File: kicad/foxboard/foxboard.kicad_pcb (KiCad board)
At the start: 2 copper layers, 360.7 x 139.7 mm, 183 parts, among them J2 USB_C_Receptacle_USB2.0, K1 KEYSW, K10 KEYSW, K11 KEYSW, K12 KEYSW, K13 KEYSW, K14 KEYSW, K15 KEYSW, K16 KEYSW, K17 KEYSW, K18 KEYSW, K19 KEYSW, K2 KEYSW, K20 KEYSW, K21 KEYSW, K22 KEYSW, K23 KEYSW, K24 KEYSW, K25 KEYSW, K26 KEYSW, K27 KEYSW, K28 KEYSW, K29 KEYSW, K3 KEYSW, K30 KEYSW, K31 KEYSW, K32 KEYSW, K33 KEYSW, K34 KEYSW, K35 KEYSW, K36 KEYSW, K37 KEYSW, K38 KEYSW, K39 KEYSW, K4 KEYSW, K40 KEYSW, K41 KEYSW, K42 KEYSW, K43 KEYSW, K44 KEYSW, K45 KEYSW, K46 KEYSW, K47 KEYSW, K48 KEYSW, K49 KEYSW, K5 KEYSW, K50 KEYSW, K51 KEYSW, K52 KEYSW, K53 KEYSW, K54 KEYSW, K55 KEYSW, K56 KEYSW, K57 KEYSW, K58 KEYSW, K59 KEYSW, K6 KEYSW, K60 KEYSW, K61 KEYSW, K62 KEYSW, K63 KEYSW, K64 KEYSW, K65 KEYSW, K66 KEYSW, K67 KEYSW, K68 KEYSW, K69 KEYSW, K7 KEYSW, K70 KEYSW, K71 KEYSW, K72 KEYSW, K73 KEYSW, K74 KEYSW, K75 KEYSW, K76 KEYSW, K77 KEYSW, K78 KEYSW, K79 KEYSW, K8 KEYSW, K80 KEYSW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

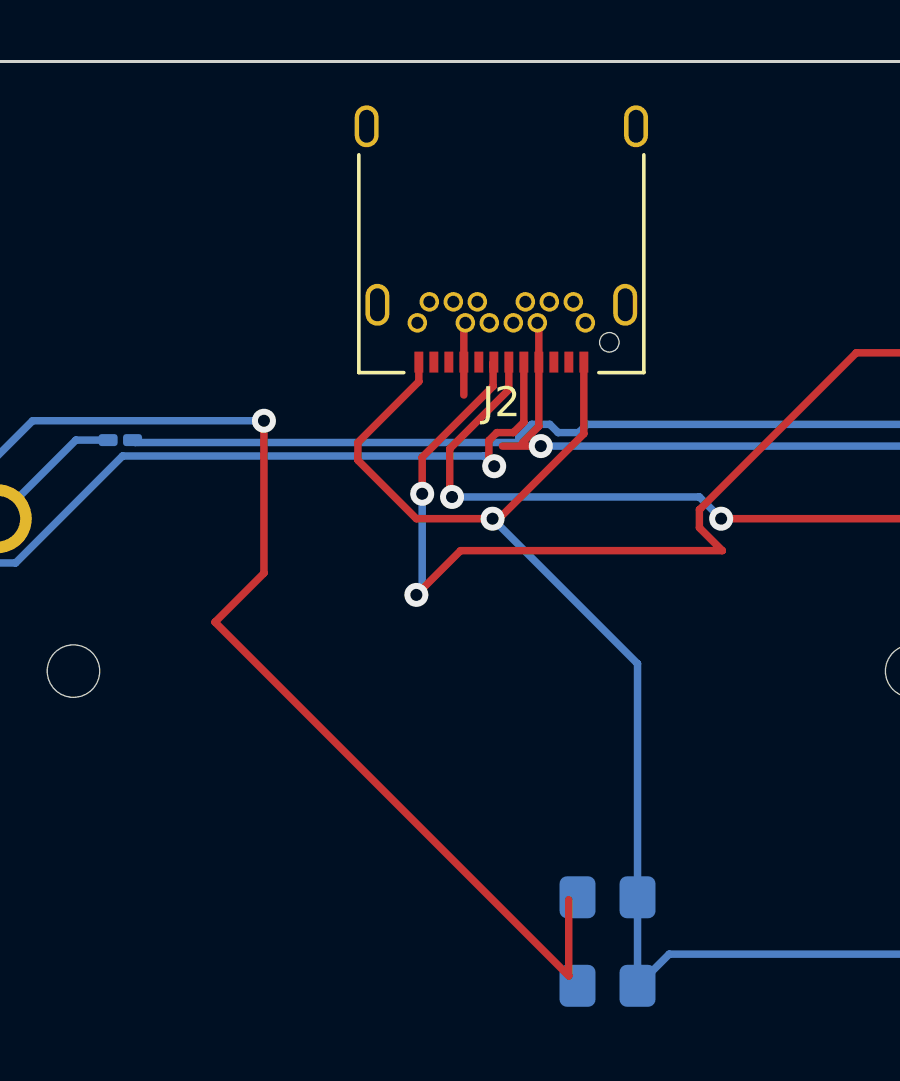
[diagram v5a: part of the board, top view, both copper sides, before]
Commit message: use usbc 2.0 recepticale
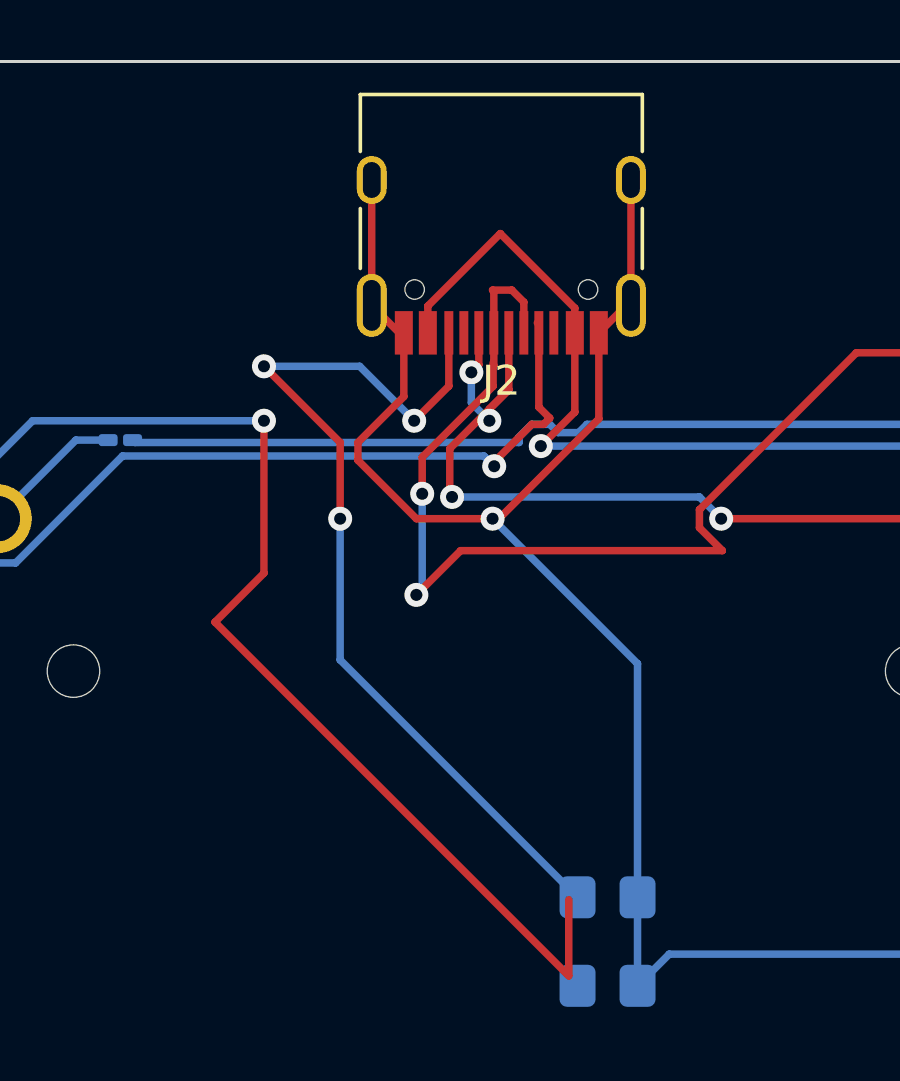
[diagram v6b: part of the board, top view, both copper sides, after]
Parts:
- J2: footprint Connector_USB:USB_C_Receptacle_Amphenol_12401548E4-2A -> Connector_USB:USB_C_Receptacle_HRO_TYPE-C-31-M-12
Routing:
- net Net-(J2-CC2): track 0.00 -> 31.2 mm, vias 0 -> 3
- net GND: track 402.1 -> 415.3 mm
- net Net-(J2-D+-PadA6): track 400.7 -> 406.3 mm, vias 3 -> 5
- net VBUS: track 405.5 -> 410.4 mm
- net Net-(J2-D--PadA7): track 424.7 -> 429.5 mm
- net Net-(J2-CC1): track 63.7 -> 65.0 mm

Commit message: add fill
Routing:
- net row 2: track 401.6 -> 403.5 mm
- net Net-(J2-CC1): track 65.0 -> 64.8 mm, vias 2 -> 3
- added copper zone on F.Cu, net GND

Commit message: update
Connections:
- U2 pad 43: unconnected-(U2-21_A7_RX5_BCLK1-Pad43) -> row 3
- U2 pad 44: row 3 -> row 2
- U2 pad 45: row 2 -> row 1
- U2 pad 46: row 1 -> unconnected-(U2-3V3-Pad46)
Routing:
- net row 2: track 403.5 -> 405.9 mm
- net row 1: track 419.9 -> 421.3 mm
- net row 3: track 392.6 -> 393.5 mm
- net VBUS: track 410.4 -> 410.5 mm, vias 3 -> 4
- added copper zone on B.Cu, net GND
- added copper zone on F.Cu, net VBUS
- removed copper zone on F.Cu, net GND
